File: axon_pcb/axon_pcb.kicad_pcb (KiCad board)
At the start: 2 copper layers, 227.6 x 99.2 mm, 125 parts, among them J1 USB_C_Receptacle, J2 AVR_ISP Header, K1 KEYSW, K10 KEYSW, K11 KEYSW, K12 KEYSW, K13 KEYSW, K14 KEYSW, K15 KEYSW, K16 KEYSW, K17 KEYSW, K18 KEYSW, K19 KEYSW, K2 KEYSW, K20 KEYSW, K21 KEYSW, K22 KEYSW, K23 KEYSW, K24 KEYSW, K25 KEYSW, K26 KEYSW, K27 KEYSW, K28 KEYSW, K29 KEYSW, K3 KEYSW, K30 KEYSW, K31 KEYSW, K32 KEYSW, K33 KEYSW, K34 KEYSW, K35 KEYSW, K36 KEYSW, K37 KEYSW, K38 KEYSW, K39 KEYSW, K4 KEYSW, K40 KEYSW, K41 KEYSW, K42 KEYSW, K43 KEYSW, K44 KEYSW, K45 KEYSW, K46 KEYSW, K5 KEYSW, K6 KEYSW, K7 KEYSW, K8 KEYSW, K9 KEYSW, SW1 RESET, SW2 BOOT, U1 ATmega328P-PU, X1 16MHz

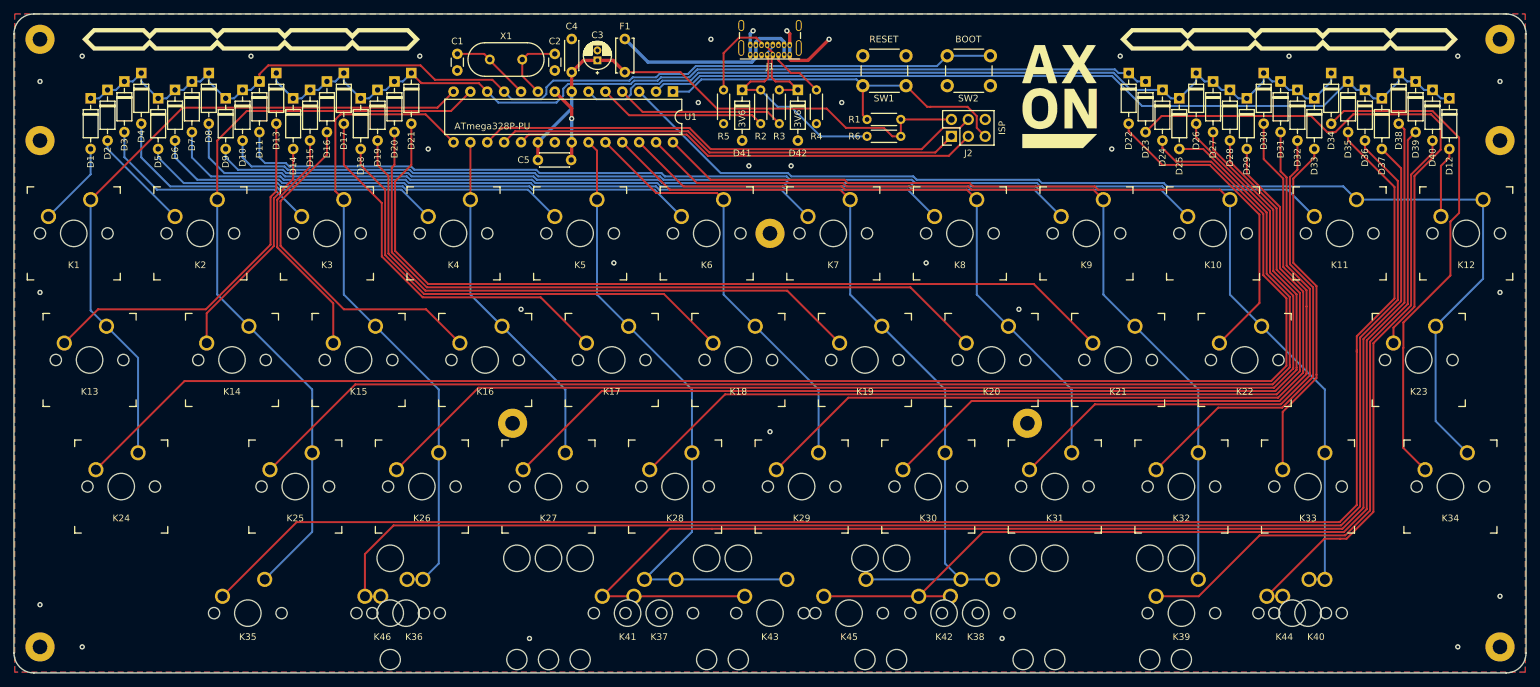
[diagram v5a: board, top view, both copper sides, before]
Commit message: slight position and shape changes
- matched corner rounding to hole position
- tweaked crystal caps position to be symmetric about crystal
- tweaked hole positions to be more accurate
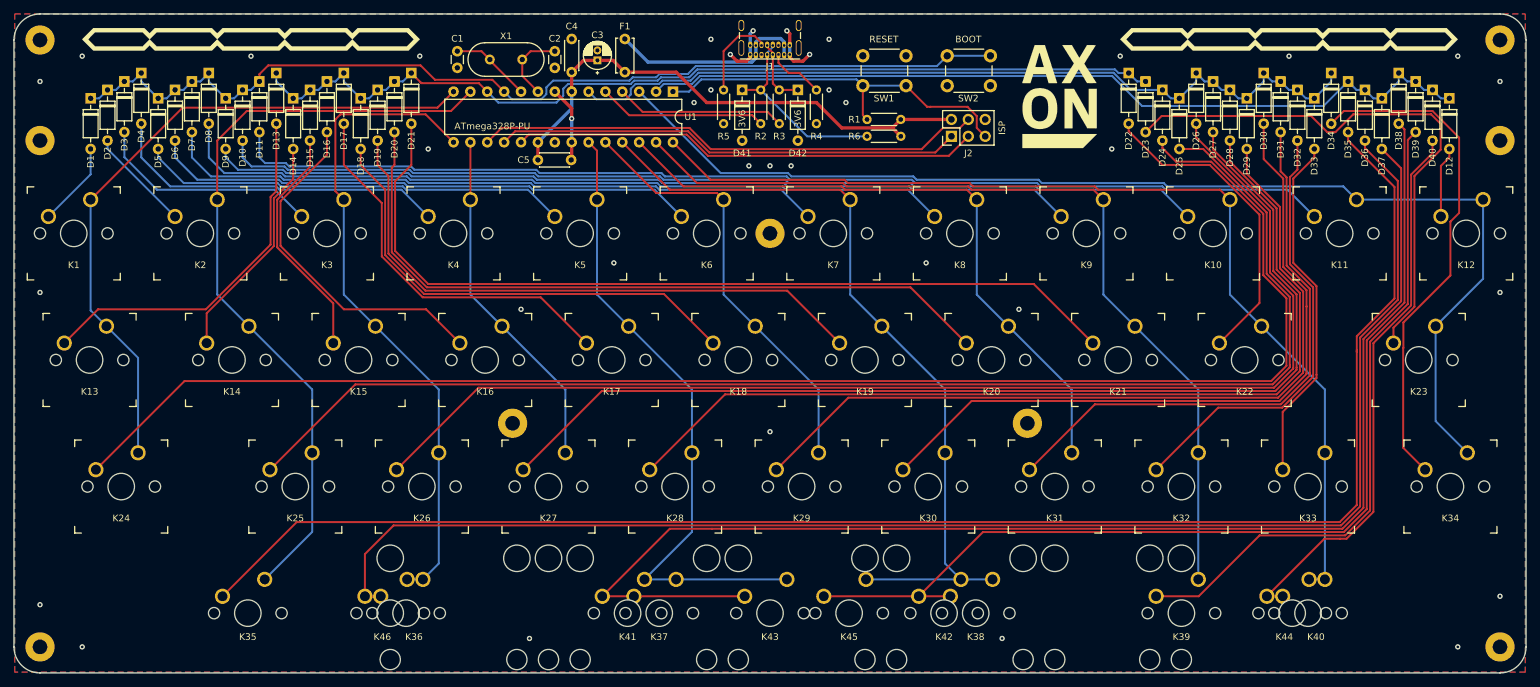
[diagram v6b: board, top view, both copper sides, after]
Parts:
- moved C1 0.40 mm to (57.7, -27.4)
- moved C2 0.40 mm to (72.4, -27.4)
- moved REF** 0.11 mm to (214.6, -29.1)
- moved REF** 0.11 mm to (-5.08, -29.1)
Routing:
- net /D+: track 12.7 -> 10.2 mm
- net /D-: track 31.0 -> 29.1 mm
- net +5V: track 80.5 -> 79.7 mm
- net GND: track 26.8 -> 27.0 mm, vias 32 -> 37
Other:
- outline, holes or cut-outs redrawn

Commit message: add power LED
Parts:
- added D43: LED, LED_THT:LED_D5.0mm, F.Cu at (124.0, -14.9)
- added R7: 300, Resistor_THT:R_Axial_DIN0204_L3.6mm_D1.6mm_P5.08mm_Horizontal, F.Cu at (119.3, -18.7)
- moved R6 29.0 mm to (95.5, -16.5), turned to 90 degrees
- moved R5 13.7 mm to (111.5, -16.5)
- moved R1 6.85 mm to (114.2, -21.6), turned to 270 degrees
- moved R3 5.46 mm to (100.7, -16.5)
- moved R2 5.21 mm to (98.2, -16.5)
- moved R4 2.92 mm to (108.8, -16.5)
- moved D41 2.79 mm to (103.4, -21.6)
- moved D42 2.79 mm to (106.2, -21.6)
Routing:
- net /D-: track 29.1 -> 16.2 mm
- net /USB_D+: track 25.6 -> 20.2 mm
- net Net-(D43-Pad2): track 0.00 -> 5.23 mm
- net /USB_D-: track 25.4 -> 20.2 mm
- net /RESET: track 57.7 -> 54.0 mm
- net /D+: track 10.2 -> 13.9 mm
- net +5V: track 79.7 -> 83.1 mm, vias 0 -> 1
- net Net-(J1-PadB5): track 13.7 -> 16.0 mm
- net Net-(J1-PadA5): track 8.67 -> 6.49 mm
- net GND: vias 37 -> 35

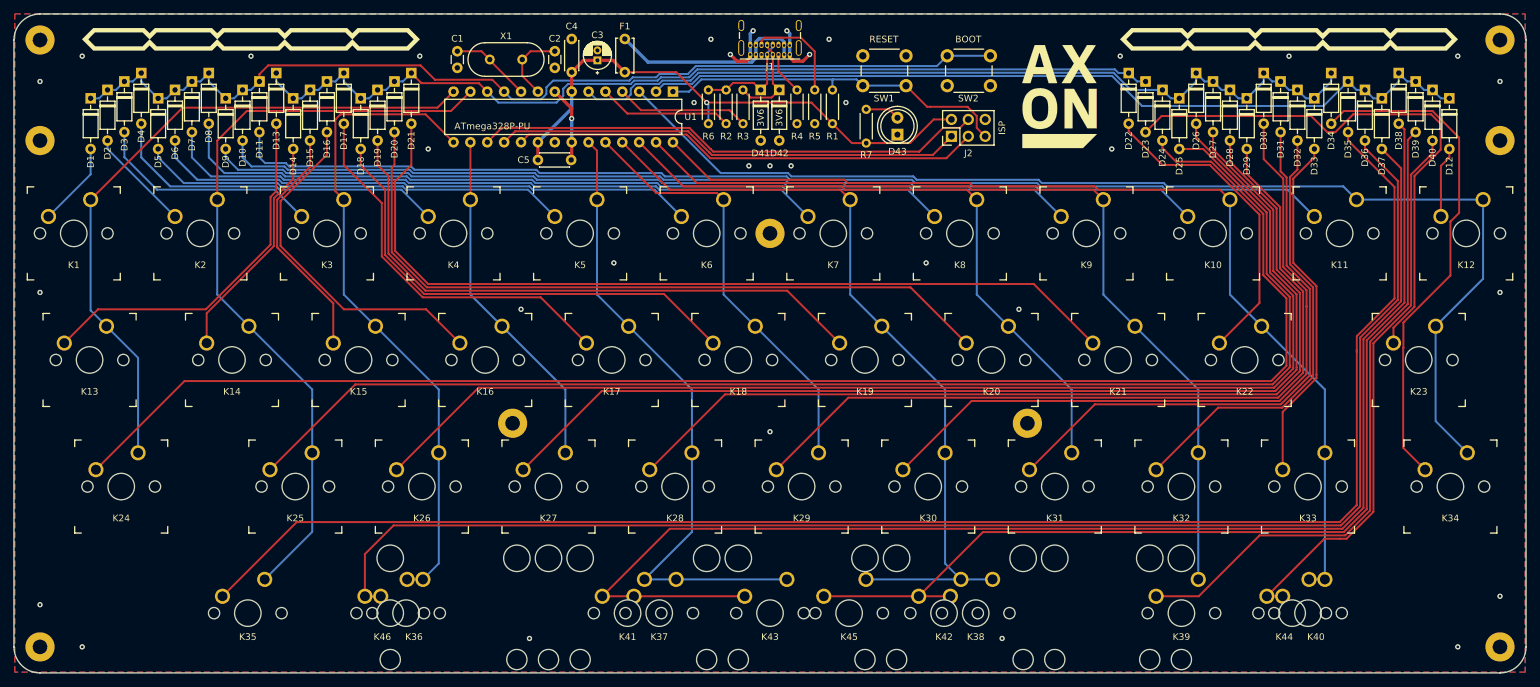
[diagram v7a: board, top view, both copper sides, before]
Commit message: update rear pcb outline
and updated .gitignore while I was at it.
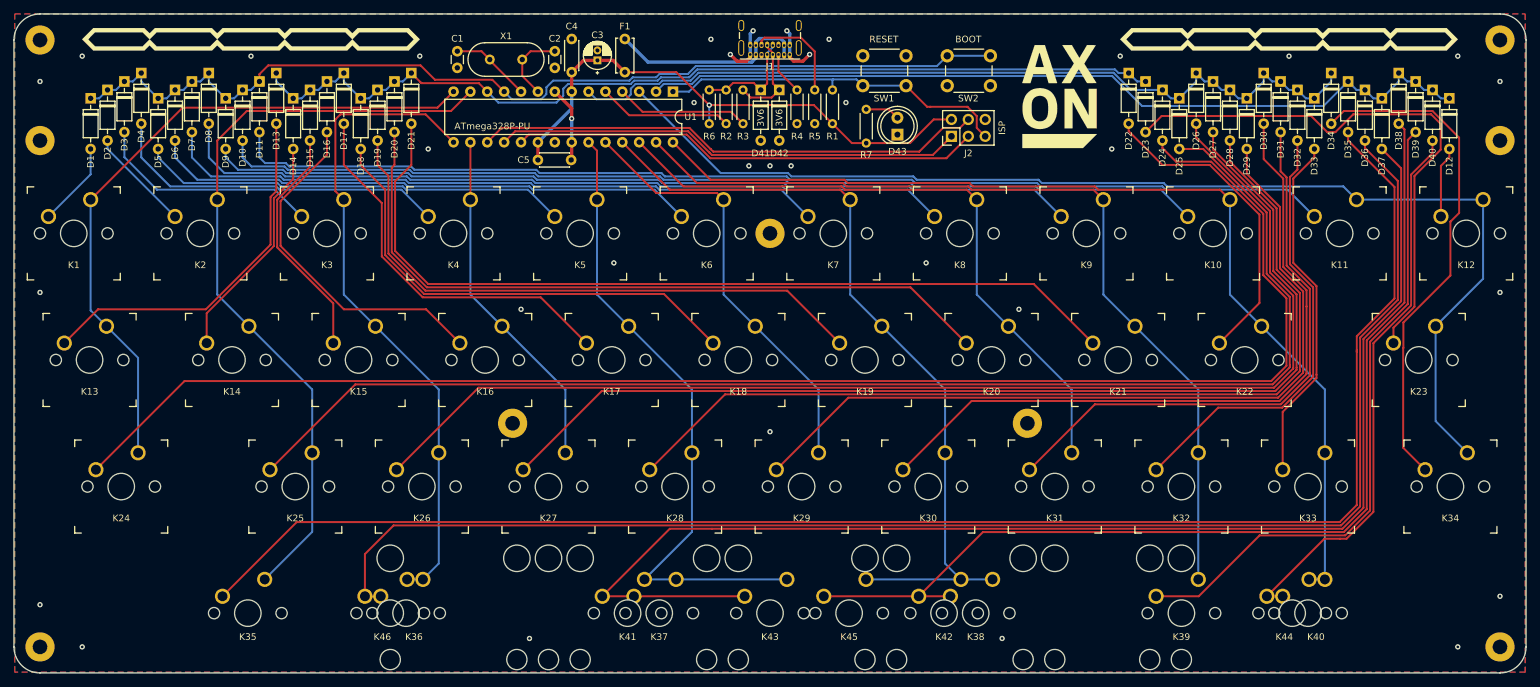
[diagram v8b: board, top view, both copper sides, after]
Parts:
- moved R6 0.13 mm to (95.6, -16.5)
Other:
- net class Default removed
